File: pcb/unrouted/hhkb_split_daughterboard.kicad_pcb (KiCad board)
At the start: 2 copper layers, 21 x 32 mm, 11 parts

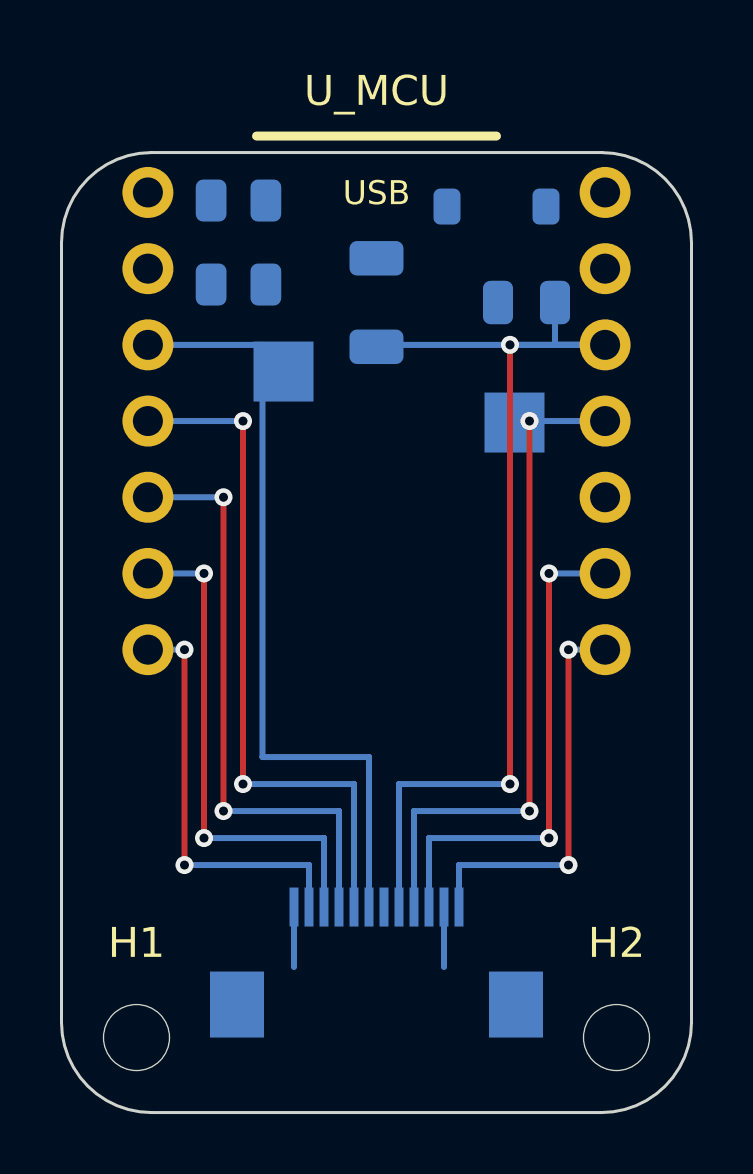
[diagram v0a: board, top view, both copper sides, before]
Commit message: 子基板の配線を外周へ逃がし、電源部の向きを流れに合わせた
利用者が絵で示した「電源は盤面の外周を使い、中央を空ける」という
方針を実装した回。**私は数字だけ追っていて、絵を見た利用者の指摘の
ほうが毎回早く核心に届いた。**

■ 外周レーン（利用者「両側 2 ピンぐらいは外側から回せるのでは」）

  XIAO のパッド列（±7.62）の外に **2.03mm** ある。ここへ 2 本/側を
  逃がし、内側レーンを 5 本 → 2 本に減らした。

  ⚠️ **刻みはビアの径で決まる。**最初 0.4mm（配線の幅）で 3 本置いて
  DRC 13 件。φ0.6 + クリアランス 0.2 = **0.80mm 必要**で 2 本/側が上限。

  ⚠️ **ビアを省いて裏面のまま走らせる案は駄目。**間隔 0.40mm で 3 本
  入る（外周に裏面部品は無い）が、**層の分離を失う**。内側レーンへ
  向かう横枝は B.Cu なので、外側も B.Cu だと必ず交差する（実測 12 件）。
  **ビアは無駄ではなく、層を分けるために要る。**

■ 真下パス（利用者「D6/D7 は横向きでなく下向きに伸ばせる」）

  FFC に最も近い 1 本は、パッド列の x のまま真下へ降ろす。
  レーンもビアも使わない。ROW2 18.9→16.8mm、CS 18.4→16.2mm。

  ⚠️ 条件を `|x| > 7.0` で書いて**全パッドが該当**し、20mm の配線が
  盤面を横断して DRC 38 件。正しくは「その列で FFC に最も近い 1 本」
  ＝ i == 0。

■ 部品の向き（利用者「バルクの向きが逆」「電源周りこんな感じで」）

  - C_BULK: 縦置き（x 方向 1.4mm 節約）＋ **+90°**。XIAO は 3V3 が
    手前(9.59)・GND が奥(12.13) なので、同じ並びにして平行に届かせる
  - R_LO: 180°。SENSE が R_HI 側（左）を向き、分圧の中点が隣り合う
  - SW_PWR: 中央の縦帯（x ±0.9）を空ける。GND スティッチングが使う

■ 配線長

  子基板の合計 218.5 → **205.1mm**

DRC: 左 違反3/未配線0 / 右 違反2/未配線0 / 子基板 違反6/未配線1
（主基板は**両方とも未配線 0**。子基板の 6 件は下記）
test_circuit・test_daughterboard・test_keyscan・test_schematic・
test_pinmap = 81 件通過。**pytest tools 全体は未実行。**

Co-Authored-By: Claude Opus 5 (1M context) <noreply@anthropic.com>
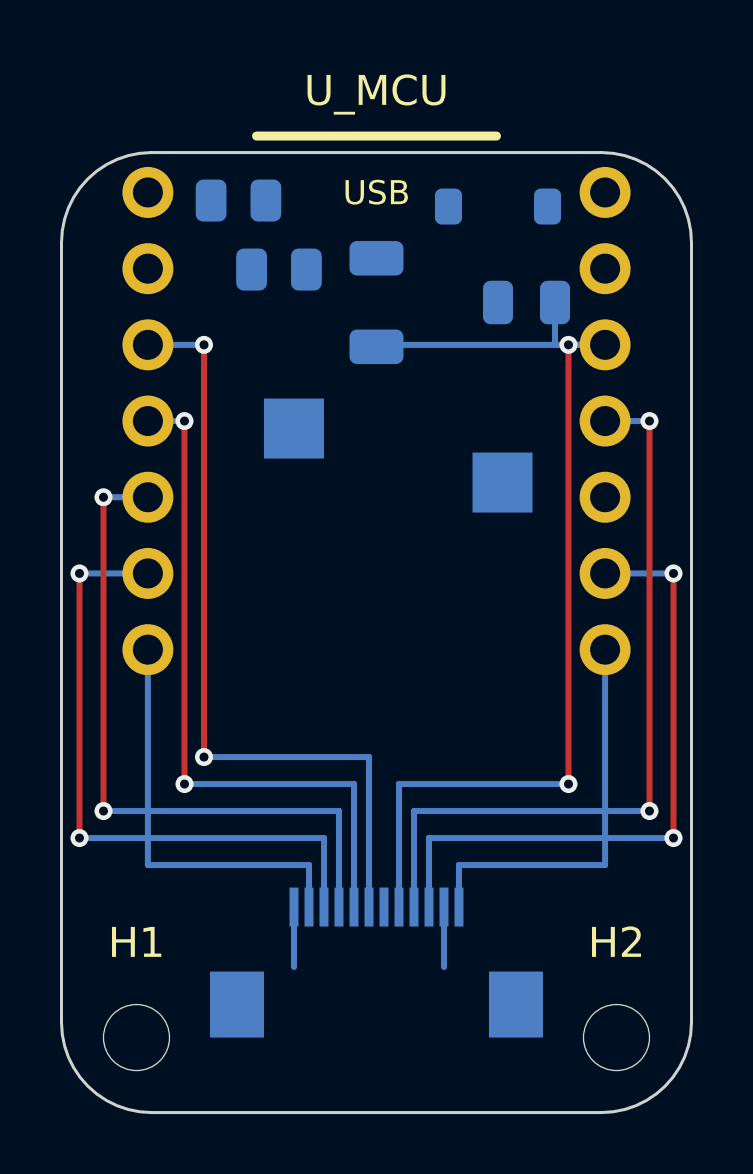
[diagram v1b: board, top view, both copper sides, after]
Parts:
- moved BT1_- 2.04 mm to (154.2, 95.0)
- moved SW_PWR_1 1.93 mm to (147.2, 93.2)
- moved R_LO 1.44 mm to (146.8, 87.9), turned to 0 degrees
- moved D_PWR 0.05 mm to (154.1, 85.8)
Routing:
- net SPI_SCK: track 17.0 -> 21.6 mm
- net ROW3: track 17.0 -> 21.6 mm
- net SPI_MOSI: track 22.6 -> 25.5 mm
- net ROW4: track 20.0 -> 23.0 mm
- net ROW2: vias 2 -> 0
- net ROW0: vias 0 -> 2
- net CS: vias 2 -> 0

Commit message: 警告を数え、浮いた GND を辿って消し、FFC の地面を繋いだ
DRC の「違反 0」がエラーだけの数だった。--severity-error を外し、
警告を別の数として記録・表示する。左 35 / 右 48 / 子基板 24、
合計 107 件がそれまで構造的に見えなかった。合否はエラーだけで
決める（警告を混ぜると、MX フットプリントが持つ穴の間隔で
34 件が永久に赤になり、直せない赤が新しい赤を隠す）。

浮いた GND の判定が「区画の中にビアかパッドがあるか」だった。
それではビアの行き先を見ておらず、右基板では 23 区画すべてが
「浮いていない」と答えるのに DRC は未配線を報告していた。
ベタ・配線・ビアを同じ連結成分に載せ、本土へ辿り着けないものを
浮きとする。ベタだけ消すと配線とビアが残って宙に浮くので、
三者まとめて名指しで消す（面積の閾値では分けられない。浮きの
最大 3.01mm² が、繋がっている島の最小 1.51mm² より大きい）。

MAX_FLOATING_ISLANDS が同じファイルに 2 回定義されていて、
後の 12 が勝っていた。「0 でなければならない」と書いた検査が、
12 個まで黙って通していた。古い方を消す。

ELEC_REF に J_MAIN が無く、FFC の GND パッドにビアが打たれて
いなかった。J_DB だけあって対の J_MAIN が無い。対で書く。
主基板 2 枚に影響は無い（J_MAIN は子基板にしかない）。

穴を障害物に入れていなかった。パッドの外接箱は銅の広がりで、
NPTH の穴を表せない。要求される距離も違う（銅 0.2 対 穴 0.5）。
GND ビアがスイッチの穴に 0.479mm まで寄っていた。

子基板の V3V3 を FFC から電源群へ繋いだ。列の下へ降りて外へ
出てから上がる。降りる高さも外へ出る位置も、GND ビアと
取り付けパッドの実位置から計算する（固定値で書いて 3 度当てた）。

子基板 未配線 1 → 0。残る違反 1 件は gen_daughterboard が
gnd_fanout.place を呼ばず、Freerouting に渡す時点でビアが
存在しないため避けようがない件。順序の設計に関わるので別で扱う。

left / right の基板は再生成していない（今日のコード変更が
反映されていないので、記録だけ更新して現物は次回に回す）。

Co-Authored-By: Claude Opus 5 (1M context) <noreply@anthropic.com>
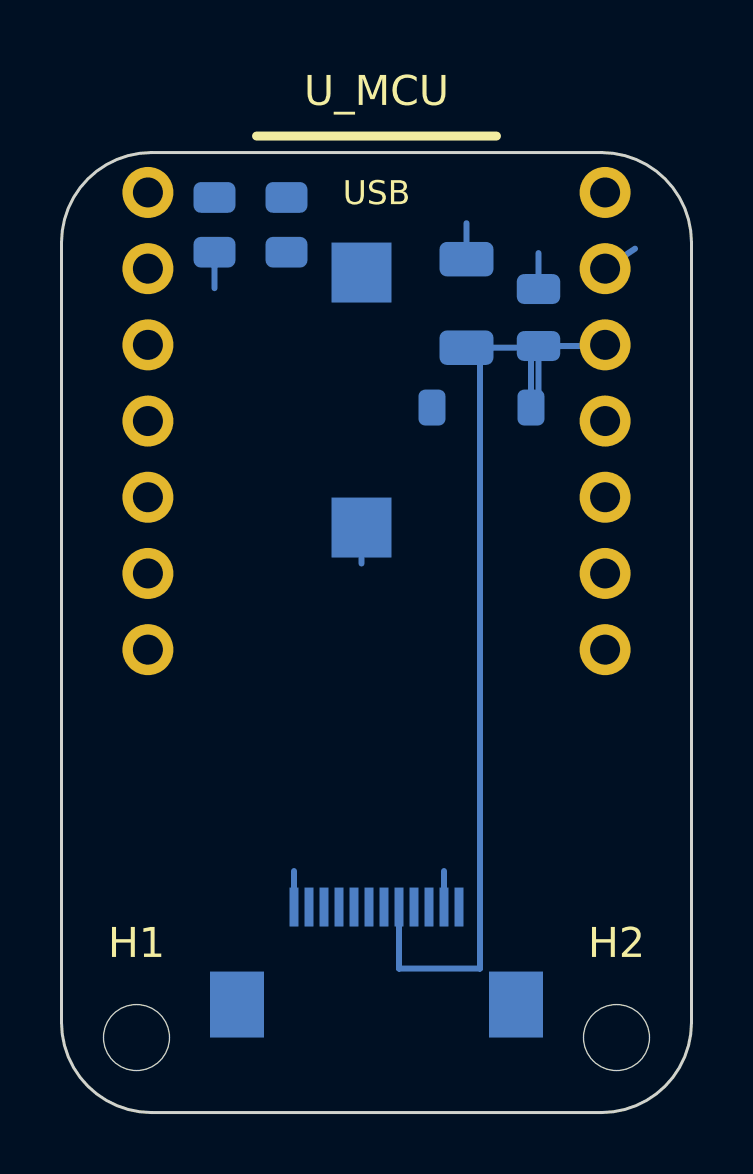
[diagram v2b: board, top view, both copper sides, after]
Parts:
- moved D_PWR 6.72 mm to (153.5, 92.5)
- moved SW_PWR_1 5.67 mm to (149.5, 88.0)
- moved BT1_- 4.93 mm to (149.5, 96.5)
- moved C_BULK 3.00 mm to (153.0, 89.0)
- moved R_LO 2.62 mm to (144.6, 86.4), turned to -90 degrees
- moved R_HI 1.79 mm to (147.0, 86.4), turned to 90 degrees
- moved C_DB 0.64 mm to (155.4, 89.5), turned to 90 degrees
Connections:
- U_MCU pad D3: ROW1 -> ROW2
- U_MCU pad D4: ROW4 -> ROW3
- U_MCU pad D5: ROW3 -> ROW4
- U_MCU pad D6: ROW2 -> ROW1
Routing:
- net ROW0: track 26.1 -> 0.00 mm, vias 2 -> 0
- net SPI_MOSI: track 25.5 -> 0.00 mm, vias 2 -> 0
- net ROW1: track 23.1 -> 0.00 mm, vias 2 -> 0
- net ROW4: track 23.0 -> 0.00 mm, vias 2 -> 0
- net SPI_SCK: track 21.6 -> 0.00 mm, vias 2 -> 0
- net ROW3: track 21.6 -> 0.00 mm, vias 2 -> 0
- net ROW2: track 14.0 -> 0.00 mm
- net CS: track 13.5 -> 0.00 mm
- net GND: track 4.00 -> 8.40 mm
- net V3V3: track 36.4 -> 34.6 mm, vias 2 -> 0

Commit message: 子基板の DRC を 0 にし、行を XIAO パッドの外周へ自分で引いた
**DRC のエラー 1 件は、子基板だけ GND ファンアウトを配線前に打って
いなかったのが原因だった。**主基板は gen_pcb が配置段階で
`gnd_fanout.place` を呼ぶのでビアが DSN に載り、Freerouting が避ける
（未配線の左 5 個・右 10 個）。**子基板は 0 個**だったのに、autoroute は
「配線前と同じ位置に戻るので衝突しない」と書いていた。前提が成立して
おらず、空き地と思って引かれた ROW1 の上にあとからビアが立っていた
（0.0091mm ＝ 実質短絡）。gen_daughterboard にも同じ一手を足した。

**ROW2/3/4 を XIAO のパッド列の外側へ、自分で引くようにした**（利用者
「D3〜D5 を外側に。D3 = ROW2 が最も外周側」）。

この並び自体は前からあったが、**絵に描いた餅だった。**配線後の基板を
実測すると列の外へ出ていたのは 2 本だけで、ROW3/ROW4 はパッド
（x=-7.62）で止まり、内側にいるはずの ROW0 が外周を取っていた。
自動配線器はこの計画を知らない。`_prewire_rows` で引いて実現した
（実測 x=-10.10/-9.70/-9.30・交差 0・斜め 0）。

**経路は L 字 3 回だけ。**一度は「上へ→左へ→下へ→左へ→上へ」と 5 回
折れていた（利用者「クネクネ迂回はやめて。最短で」）。中ほどの上下は
12 番 GND の引き出しが列の内側へ伸びていた頃の名残で、**その引き出しを
列の外側（下）へ向けた時点で不要になっていた。**消して 3 本の総長が
83.37 → **71.07mm**（各行とも外周経由の最短と一致）。

**シルクの参照名を 0.8mm に。**この基板だけ silk_overlap が 14 件あった
（主基板は 5〜6 件）。21mm 幅に電源部 5 個が固まり、8 文字の参照名が
隣に乗っていた。0.7mm は KiCad の text_height に触れるので 0.8 が下限。

    違反 1 → **0** / 未配線 0 / 警告 24 → **16**（すべてシルクの文字）

⚠️ **`PREWIRED_DB` に `ROW[234]` を足すのが対。**足さないと DSN に
未配線として残り、Freerouting が二重に引いて同じネットが自分自身と
交差する（2026-08-14 に手配線をやめた原因がこれだった）。SES 取り込みは
既存の配線を作り直すので、autoroute 側での立て直しも要る。

主基板の赤 6 件（bulk capacitor・net count・right の DRC）は**この変更の
前から**落ちている（変更を退避して確認済み）。子基板は 4 件とも通る。

Co-Authored-By: Claude Opus 5 (1M context) <noreply@anthropic.com>
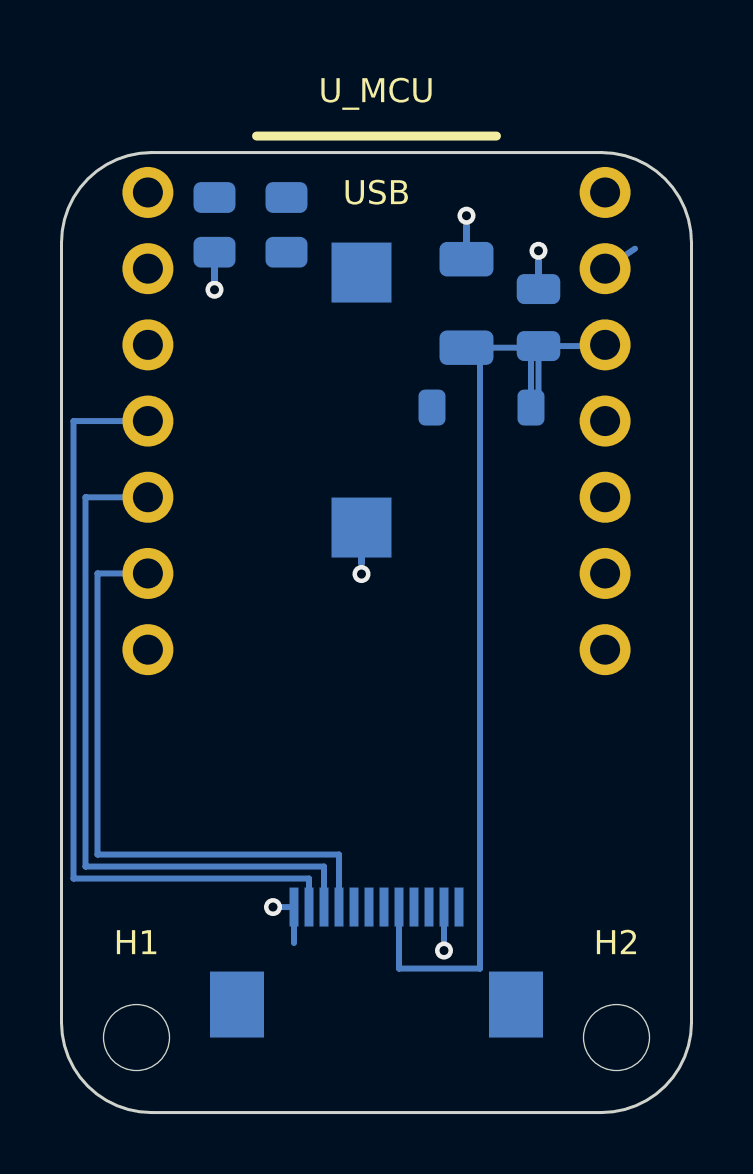
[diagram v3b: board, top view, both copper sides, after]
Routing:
- net ROW2: track 0.00 -> 26.5 mm
- net ROW3: track 0.00 -> 23.7 mm
- net ROW4: track 0.00 -> 20.9 mm
- net GND: track 8.40 -> 16.1 mm, vias 0 -> 6

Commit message: 外周レーンを板端とパッドのまん中に置いた
**配線が板の端ギリギリだった**（利用者の指摘）。ROW2 の銅から板端まで
**0.30mm ＝ 設計規則ちょうど**で、丸め 1 つで割れる余裕しかなかった。
レーンを `outer_limit`（板端 + 端クリアランス）から配っていたため。

⚠️ **パッド側へ寄せるのでは直らない。**そうすると今度は ROW4 が D6 の
パッドまで 0.20mm（これも規則ちょうど）になる（利用者「右に寄りすぎ。
D5 のラインが D6 の絶縁に被ってます」）。

⚠️ **クリアランスを足した内側で中央を取っても、まん中にならない。**
板端側は端クリアランス 0.30、パッド側は銅間クリアランス 0.20 と
**足す量が違う**ので、その差 0.10mm がそのまま偏りになる
（実測: 板端 0.56mm に対しパッド側 0.46mm）。

**障害物の縁そのもの**（板端 -10.50 と パッドの左端 -8.47）でまん中を
取り、そこへ束の中心を置く（利用者「絶縁部も含めて中央揃えが正しい
のでは」）。

    板端まで **0.515mm** / パッド縁まで **0.515mm**（差 0.000）

規則（板端 0.30・銅間 0.20）に対して両側とも 1.7〜2.6 倍。

順序と形は変えていない: ROW2 が最も外周（-9.88 / -9.49 / -9.09）、
交差 0・斜め 0・折れ 3 回。違反 0 / 未配線 0 / 警告 16。

Co-Authored-By: Claude Opus 5 (1M context) <noreply@anthropic.com>
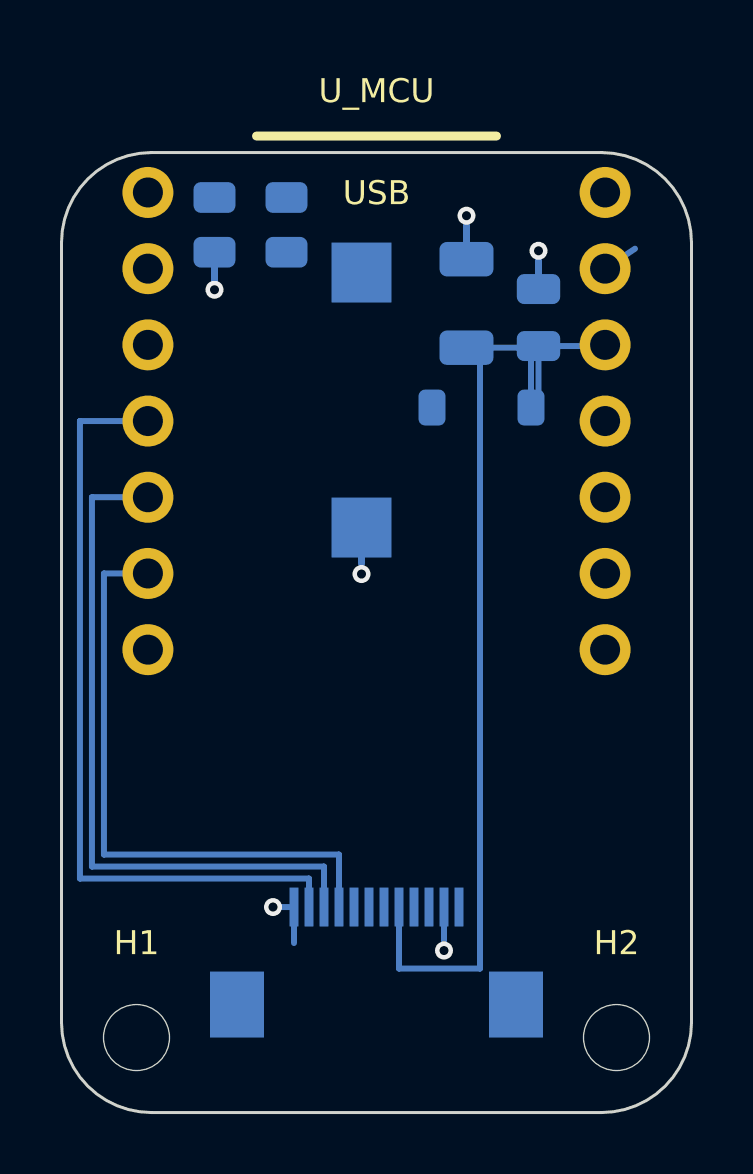
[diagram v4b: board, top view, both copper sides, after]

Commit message: D2 と D6 も列の内側を L 字で FFC へ引いた
ROW0/ROW1 は Freerouting 任せで盤面を斜めに横断していた（ROW0 は
直線 22.4mm に対し 39.1mm）。ROW2/3/4 と同じ理屈で自分で引く。

  D6（ROW1）… 垂直に下ろす → 直角に曲げて FFC へ
  D2（ROW0）… D5 と同じ 1.465mm だけ逆向き（右）へ水平に伸ばす
              → 垂直に下ろす → 直角に曲げて FFC へ

途中で 2 つ間違えたので、両方コメントに残した:

1. 横枝の帯を ROW2/3/4 と同じ lo..hi に取り、外周組の帯と FFC の
   パッドの両方より下へ降りた。縦の 2 本が横の 3 本を突き抜けて
   不要な交差が 7 件。帯は外周組より上に取る。

2.「D5 と同じ長さ」を ROW4 の水平区間の max で拾い、パッドから出る
   枝（1.465mm）ではなく FFC 近くの帯（7.835mm）を掴んだ。その先が
   BT1_- のパッドの真上で短絡。MCU のパッドに接する方だけを見る。

autoroute.PREWIRED_DB に ROW[01] を追加（protect にしないと
Freerouting が二重に引いて自己交差する）。

daughterboard: DRC 違反 0 / 未配線 0 / B.Cu 全ネットの交差 0。
左右の基板は触っていない。

Co-Authored-By: Claude Opus 5 (1M context) <noreply@anthropic.com>
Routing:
- net ROW0: track 0.00 -> 26.1 mm
- net ROW1: track 0.00 -> 15.5 mm

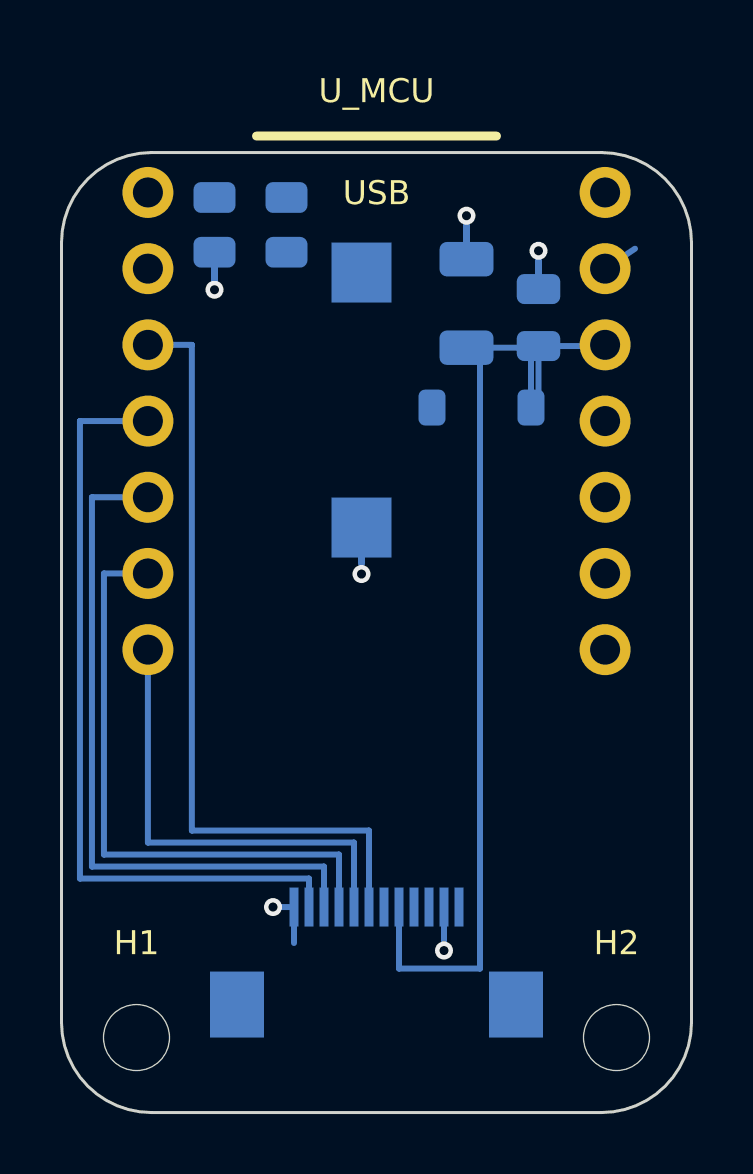
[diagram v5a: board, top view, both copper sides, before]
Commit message: 子基板の FFC 7〜12 を組み替え、レーンを XIAO のパッドで持つようにした
利用者の指定で、XIAO のパッド列の内側と外側を入れ替えた。列の外は
D1（最も板端）→ D2 → D3、内側は D6（垂直）→ D5 → D4。そのうえで
FFC の 7〜12 を 1 つずらし、載る信号を XIAO 側で吸収した。

    7 SPARE(D4) / 8 ROW3(D5) / 9 ROW4(D6)
    10 ROW1(D3) / 11 ROW2(D2) / 12 ROW0(D1)

D1 は用途未定のまま FFC 12 番まで配線だけ通す（後から線は足せない）。
GND の 2 本目は 12 番から 6 番へ移した。

レーンの表を ROW 名で持っていたのをやめ、**XIAO のパッド番号**で持つ
ようにした（OUTER_LANE_PADS / INNER_LANE_PADS / VERTICAL_PAD）。
どのレーンを通るかはパッドの話で、そこに載る信号とは無関係。ROW 名で
書いていたために、内外を入れ替えた時点で表と実物がずれ、D4 と D5 が
同じ x に降りて交差を 2 件出した。ネット名はパッドから引く。

内側が 2 本以上になったので、降りる x も帯と同じピッチでずらす。
ファームの row-gpios と決定記録の表も追随させた。

子基板 DRC: 未配線 0 / 違反 1（V3V3 と GND ビアが 0.100mm。利用者の
指示で保留）。主基板の SPARE が片側 1 ピンなので test_circuit が 2 件
赤。左右の基板は FFC が固まってから直す。

Co-Authored-By: Claude Opus 5 (1M context) <noreply@anthropic.com>
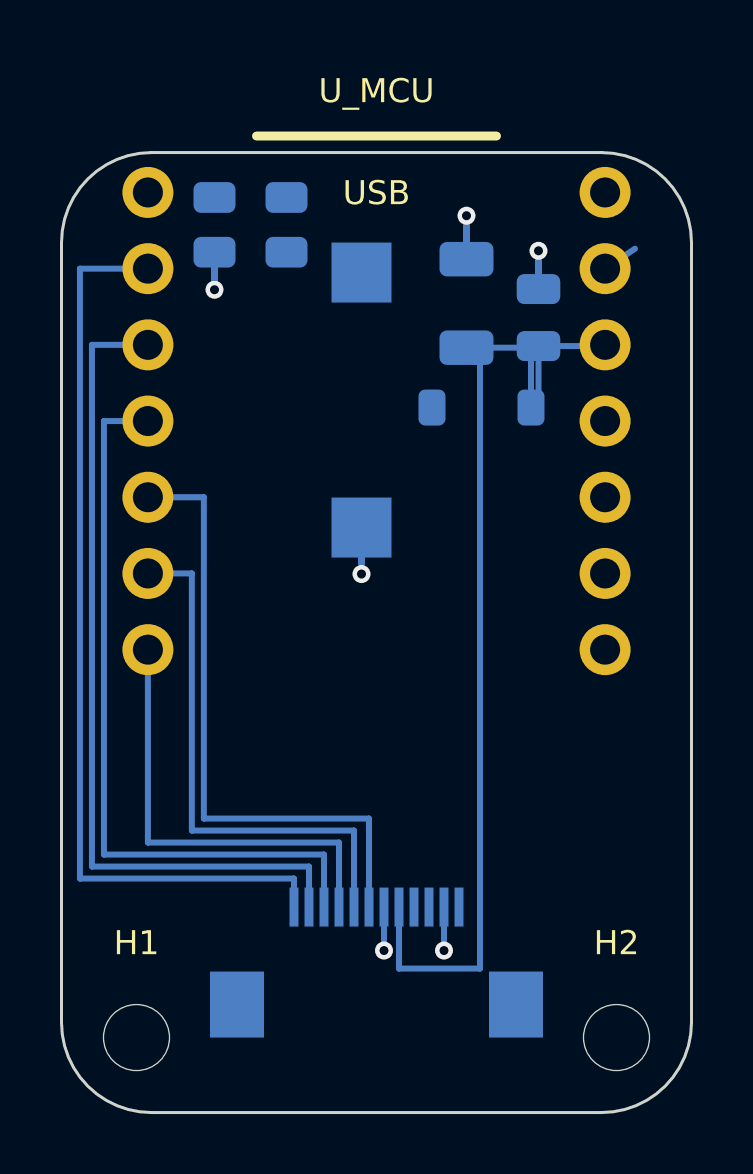
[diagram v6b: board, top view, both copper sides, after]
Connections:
- J_MAIN pad 10: ROW3 -> ROW1
- J_MAIN pad 12: GND -> ROW0
- J_MAIN pad 6: (no net) -> GND
- J_MAIN pad 7: ROW0 -> SPARE
- J_MAIN pad 8: ROW1 -> ROW3
- U_MCU pad D1: (no net) -> ROW0
- U_MCU pad D2: ROW0 -> ROW2
- U_MCU pad D3: ROW2 -> ROW1
- U_MCU pad D4: ROW3 -> SPARE
- U_MCU pad D5: ROW4 -> ROW3
- U_MCU pad D6: ROW1 -> ROW4
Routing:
- net SPARE: track 0.00 -> 21.0 mm
- net ROW1: track 15.5 -> 25.0 mm
- net ROW4: track 20.4 -> 15.0 mm
- net ROW3: track 23.3 -> 18.0 mm
- net ROW0: track 26.1 -> 30.7 mm
- net ROW2: track 26.1 -> 27.8 mm
- net GND: track 16.1 -> 16.8 mm

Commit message: 子基板の手配線の直角を、最小の 45 度 2 回に割った
利用者の指示「可能な限り最小のコーナーで 135 度 *2 に」。直角のまま
曲げると外側の角で銅が尖り、エッチングで過剰腐食を受けやすい。

点列を引く 3 か所（外側レーン・内側レーン・V3V3）が同じ形をしていたので、
面取り付きの `_polyline` に集約した。今後経路を変えても面取りは残る。

一辺は線幅と同じ 0.2mm。**見た目はほぼ角のまま**で、外側の角だけが
消えて 135 度が 2 つになる。それ以上大きくしても角の鋭さは変わらない。
線分が短くて両側に取れない折れは、その半分までに切り詰める。

実測: 45 度の区間が 20 本（配線後の基板でも 34 本残っている）。
子基板 DRC は 未配線 0 / 違反 1 で、面取りによる新しい違反は無い
（残る 1 件は V3V3 と GND ビアの 0.100mm。利用者の指示で保留中）。

Co-Authored-By: Claude Opus 5 (1M context) <noreply@anthropic.com>
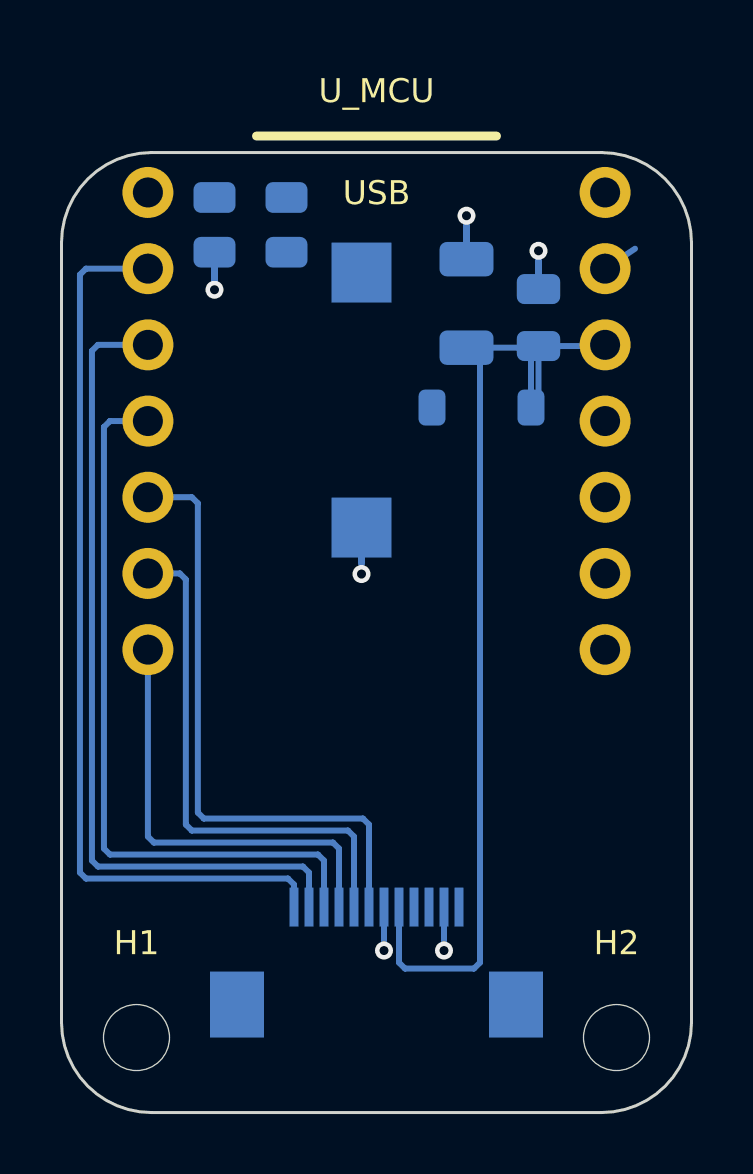
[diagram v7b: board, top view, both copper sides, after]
